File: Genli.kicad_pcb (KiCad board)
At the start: 2 copper layers, 125 x 90 mm, 20 parts, among them J1 Screw_Terminal_01x02, U1 ICM-20948, U2 VL53L0X, U3 VL53L0X

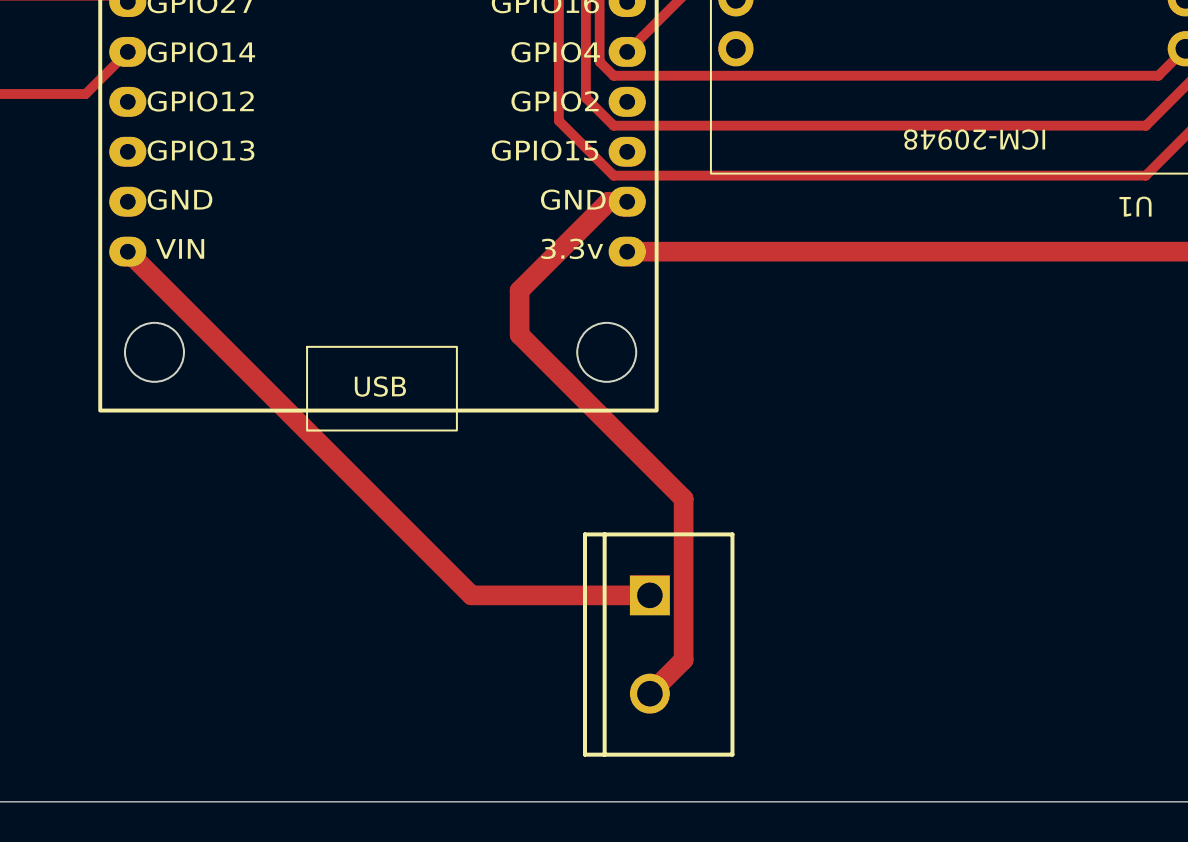
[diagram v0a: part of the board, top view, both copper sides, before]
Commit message: Save in-progress PCB layout changes
Working-tree changes that predate the repository restructure; committed as
their own change so the restructure starts from a clean tree.

Co-Authored-By: Claude Opus 5 <noreply@anthropic.com>
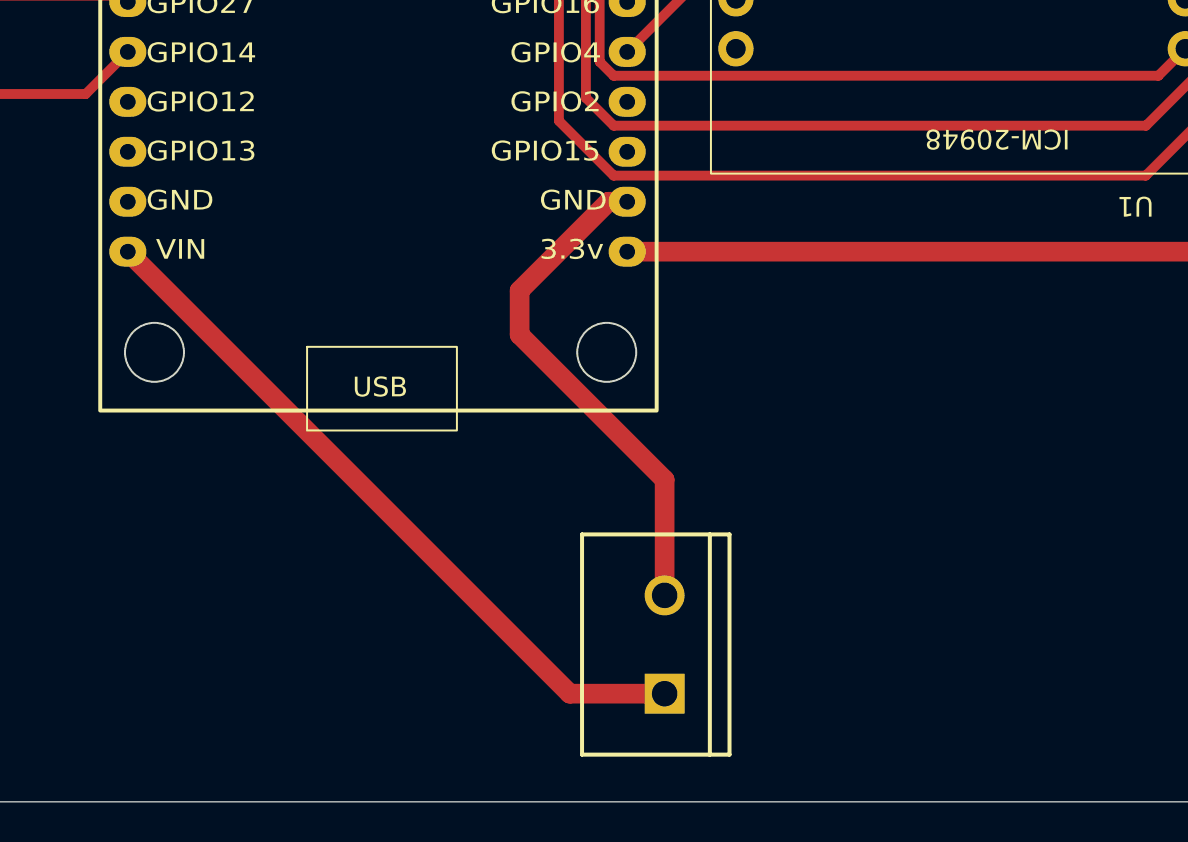
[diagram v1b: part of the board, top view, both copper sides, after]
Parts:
- moved U15 5.06 mm to (139.4, 129.5), turned to 90 degrees
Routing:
- net Net-(U15-GND): track 32.0 -> 25.9 mm
- net Net-(U10-VIN): track 33.8 -> 36.6 mm
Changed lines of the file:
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@@
 	(footprint "PCM_SparkFun-Connector:ScrewTerminal_1x02_P5.0mm"
 		(layer "F.Cu")
-		(at 138.625 124.5 -90)
+		(at 139.375 129.5 90)
 		(tags "SparkFun")
 		(property "Reference" "U15"
@@
 					(thickness 0.1)
 				)
-				(justify top)
+				(justify bottom)
 			)
 		)
@@
 					(thickness 0.1)
 				)
-				(justify top)
+				(justify bottom)
 			)
 		)
 		(property "Datasheet" ""
-			(at 0 0 270)
+			(at 0 0 90)
 			(unlocked yes)
 			(layer "F.Fab")
@@
 		)
 		(property "Description" ""
-			(at 0 0 270)
+			(at 0 0 90)
 			(unlocked yes)
 			(layer "F.Fab")
@@
 		(duplicate_pad_numbers_are_jumpers no)
 		(fp_line
-			(start -3.1 3.3)
-			(end -3.1 2.3)
+			(start 8.1 -4.2)
+			(end 8.1 2.3)
 			(stroke
 				(width 0.2032)
@@
 		)
 		(fp_line
-			(start 8.1 3.3)
-			(end -3.1 3.3)
+			(start -3.1 -4.2)
+			(end 8.1 -4.2)
 			(stroke
 				(width 0.2032)
@@
 		)
 		(fp_line
-			(start -3.1 2.3)
-			(end -3.1 -4.2)
+			(start 8.1 2.3)
+			(end -3.1 2.3)
 			(stroke
 				(width 0.2032)
@@
 		)
 		(fp_line
-			(start 8.1 2.3)
-			(end -3.1 2.3)
+			(start -3.1 2.3)
+			(end -3.1 -4.2)
 			(stroke
 				(width 0.2032)
@@
 		)
 		(fp_line
-			(start -3.1 -4.2)
-			(end 8.1 -4.2)
+			(start 8.1 3.3)
+			(end -3.1 3.3)
 			(stroke
 				(width 0.2032)
@@
 		)
 		(fp_line
-			(start 8.1 -4.2)
-			(end 8.1 2.3)
+			(start -3.1 3.3)
+			(end -3.1 2.3)
 			(stroke
 				(width 0.2032)
@@
 		)
 		(fp_line
-			(start -3.7 2.35)
-			(end -3.1 2.35)
+			(start 8.7 -4)
+			(end 8.7 -3)
 			(stroke
 				(width 0.2032)
@@
 		)
 		(fp_line
-			(start -3.7 1.35)
-			(end -3.7 2.35)
+			(start 8.1 -4)
+			(end 8.7 -4)
 			(stroke
 				(width 0.2032)
@@
 		)
 		(fp_line
-			(start -3.1 1.35)
-			(end -3.7 1.35)
+			(start 8.7 -3)
+			(end 8.1 -3)
 			(stroke
 				(width 0.2032)
@@
 		)
 		(fp_line
-			(start 8.7 -3)
-			(end 8.1 -3)
+			(start -3.1 1.35)
+			(end -3.7 1.35)
 			(stroke
 				(width 0.2032)
@@
 		)
 		(fp_line
-			(start 8.1 -4)
-			(end 8.7 -4)
+			(start -3.7 1.35)
+			(end -3.7 2.35)
 			(stroke
 				(width 0.2032)
@@
 		)
 		(fp_line
-			(start 8.7 -4)
-			(end 8.7 -3)
+			(start -3.7 2.35)
+			(end -3.1 2.35)
 			(stroke
 				(width 0.2032)
@@
 		)
 		(pad "1" thru_hole rect
-			(at 0 0 270)
+			(at 0 0 90)
 			(size 2.032 2.032)
 			(drill 1.3)
@@
 		)
 		(pad "2" thru_hole circle
-			(at 5 0 270)
+			(at 5 0 90)
 			(size 2.032 2.032)
 			(drill 1.3)
@@
 		)
 		(fp_text user "ICM-20948"
-			(at 7 -4 180)
+			(at 5.86 -4 180)
 			(unlocked yes)
 			(layer "F.SilkS")
@@
 	)
 	(segment
-		(start 138.625 124.5)
-		(end 129.552647 124.5)
+		(start 139.375 129.5)
+		(end 134.552647 129.5)
 		(width 1)
 		(layer "F.Cu")
@@
 	)
 	(segment
-		(start 129.552647 124.5)
+		(start 134.552647 129.5)
 		(end 112.07246 107.019813)
 		(width 1)
@@
 	)
 	(segment
-		(start 140.341 127.784)
-		(end 140.341 119.586534)
-		(width 1)
-		(layer "F.Cu")
-		(net "Net-(U15-GND)")
-	)
-	(segment
 		(start 136.520187 104.479813)
 		(end 137.47246 104.479813)
@@
 	)
 	(segment
-		(start 138.625 129.5)
-		(end 140.341 127.784)
+		(start 132 111.245534)
+		(end 132 109)
 		(width 1)
 		(layer "F.Cu")
@@
 	)
 	(segment
-		(start 132 111.245534)
-		(end 132 109)
+		(start 132 109)
+		(end 136.520187 104.479813)
 		(width 1)
 		(layer "F.Cu")
@@
 	)
 	(segment
-		(start 132 109)
-		(end 136.520187 104.479813)
+		(start 139.375 124.5)
+		(end 139.375 118.620534)
 		(width 1)
 		(layer "F.Cu")
@@
 	)
 	(segment
-		(start 140.341 119.586534)
+		(start 139.375 118.620534)
 		(end 132 111.245534)
 		(width 1)
